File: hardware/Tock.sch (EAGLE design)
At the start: 37 parts, among them IC1 NE555D, IC2 LM7805, IC3 AVR-MEGA8-PPTH, IC4 MCP1700-33, J2 ISP, J4 VIN, Y1 16MHz

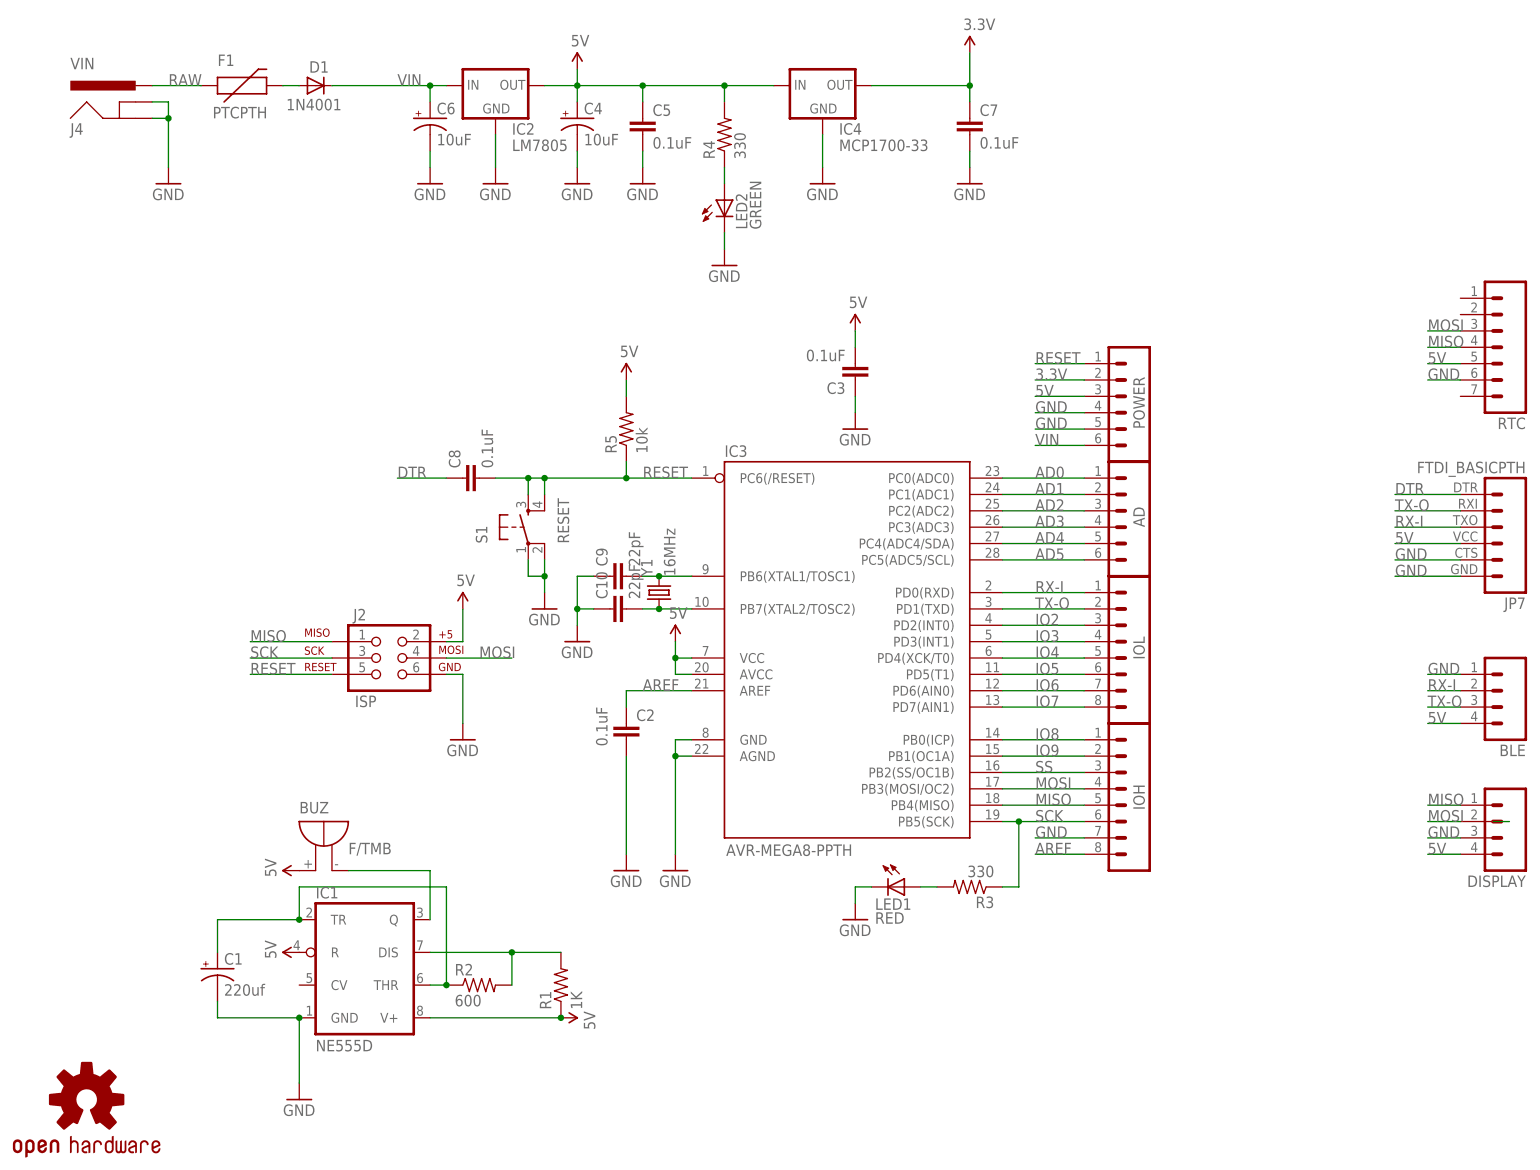
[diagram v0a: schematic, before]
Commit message: Update hardware
Remove extra bit-packing code and switch to standard library macros
Encapsulate enums
Add WIP BOM and more information to readme
Finish routing hardware
Switch to SMD capacitors and resistors
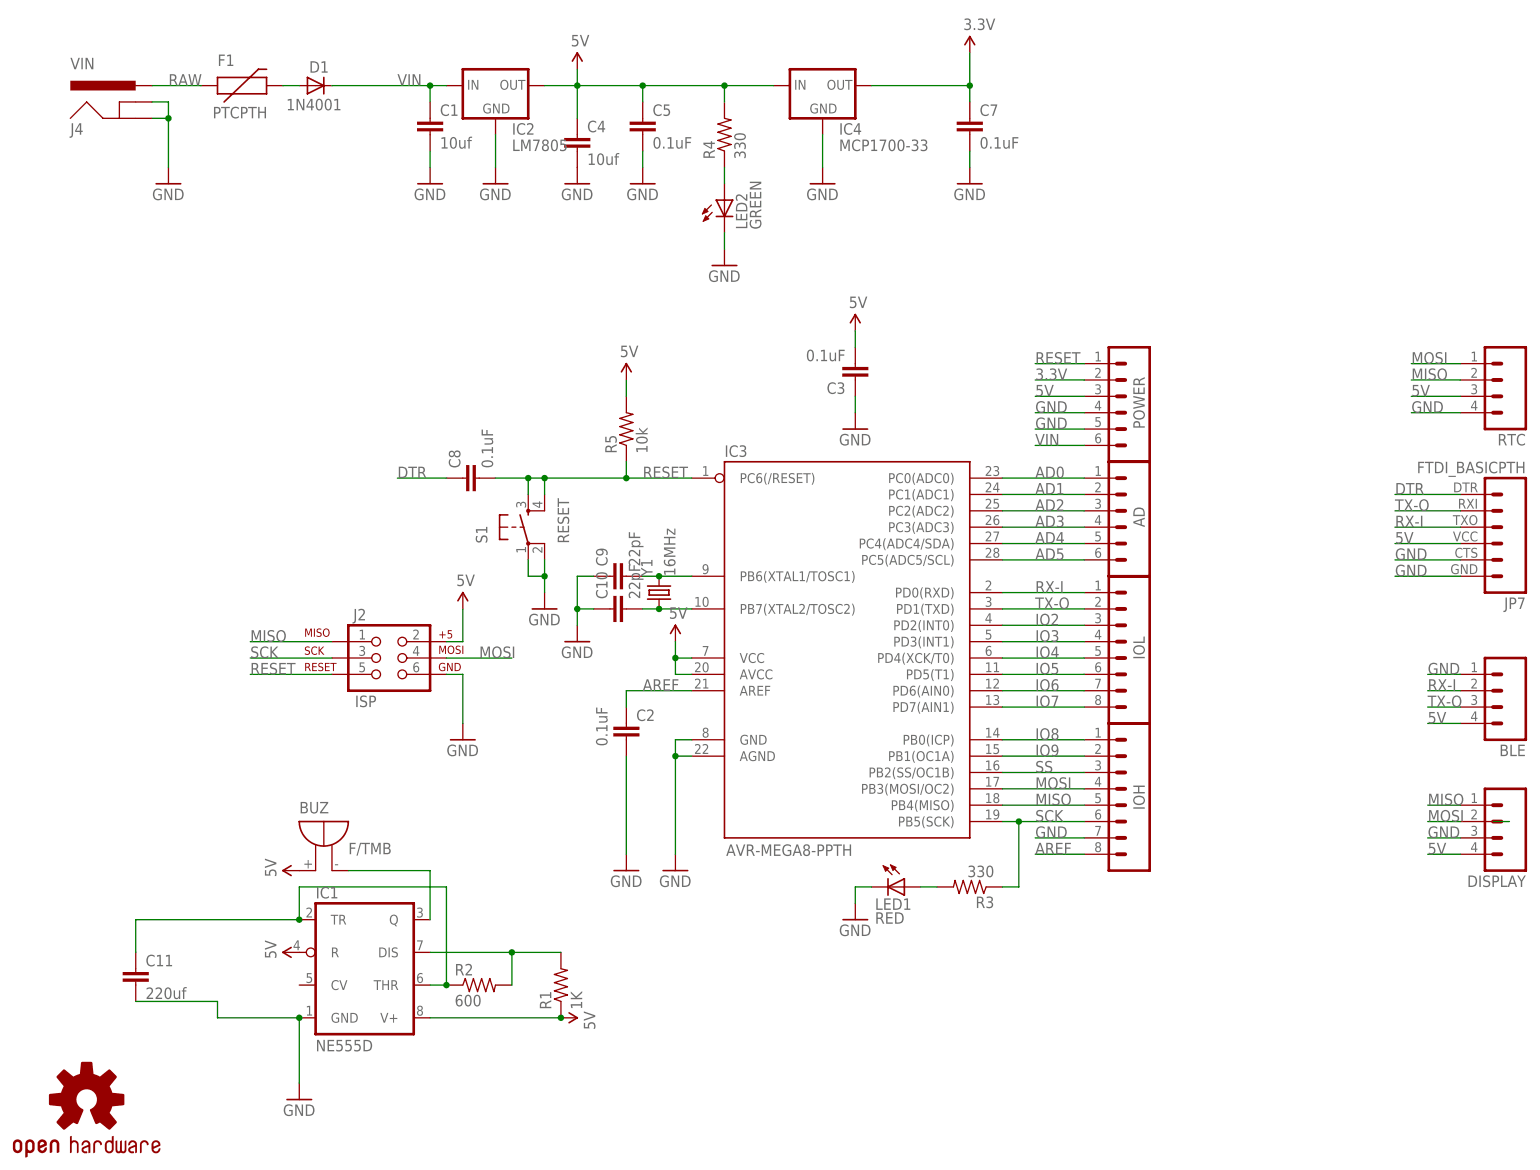
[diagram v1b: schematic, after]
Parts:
- removed C6: 10uF, SparkFun:CAP_POLPTH2
- added C11: 220uf, SparkFun-Passives:CAP0805
- AD, POWER: device SparkFun:M06SIP -> SparkFun-Connectors:M06LOCK
- C1: value 220uf -> 10uf; device rcl:CPOL-USE2.5-5 -> SparkFun-Passives:CAP0805
- C10, C2, C5, C7, C8, C9: device SparkFun:CAPPTH2 -> SparkFun-Passives:CAP0805
- C4: value 10uF -> 10uf; device SparkFun:CAP_POLPTH2 -> SparkFun-Passives:CAP0805
- IOH, IOL: device SparkFun:M081X08 -> SparkFun-Connectors:M08LOCK
- LED1, LED2: device SparkFun:LED5MM -> led:LEDCHIP-LED0805
- R1, R2: device rcl:R-US_0204/5 -> SparkFun-Resistors:RESISTOR0805-RES
- R3, R4, R5: device SparkFun:RESISTORAXIAL-0.3 -> SparkFun-Resistors:RESISTOR0805-RES
- RTC: device SparkFun-Connectors:M07LOCK -> SparkFun-Connectors:M04LOCK
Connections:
- net 5V: now also C4.1, RTC.3; no longer C4.+, RTC.5
- net GND: now also C1.2, C11.2, C4.2, RTC.4; no longer C1.-, C4.-, C6.-, RTC.6
- net MISO: now also RTC.2; no longer RTC.4
- net MOSI: now also RTC.1; no longer RTC.3
- net N$5: now also C11.1; no longer C1.+
- net VIN: now also C1.1; no longer C6.+

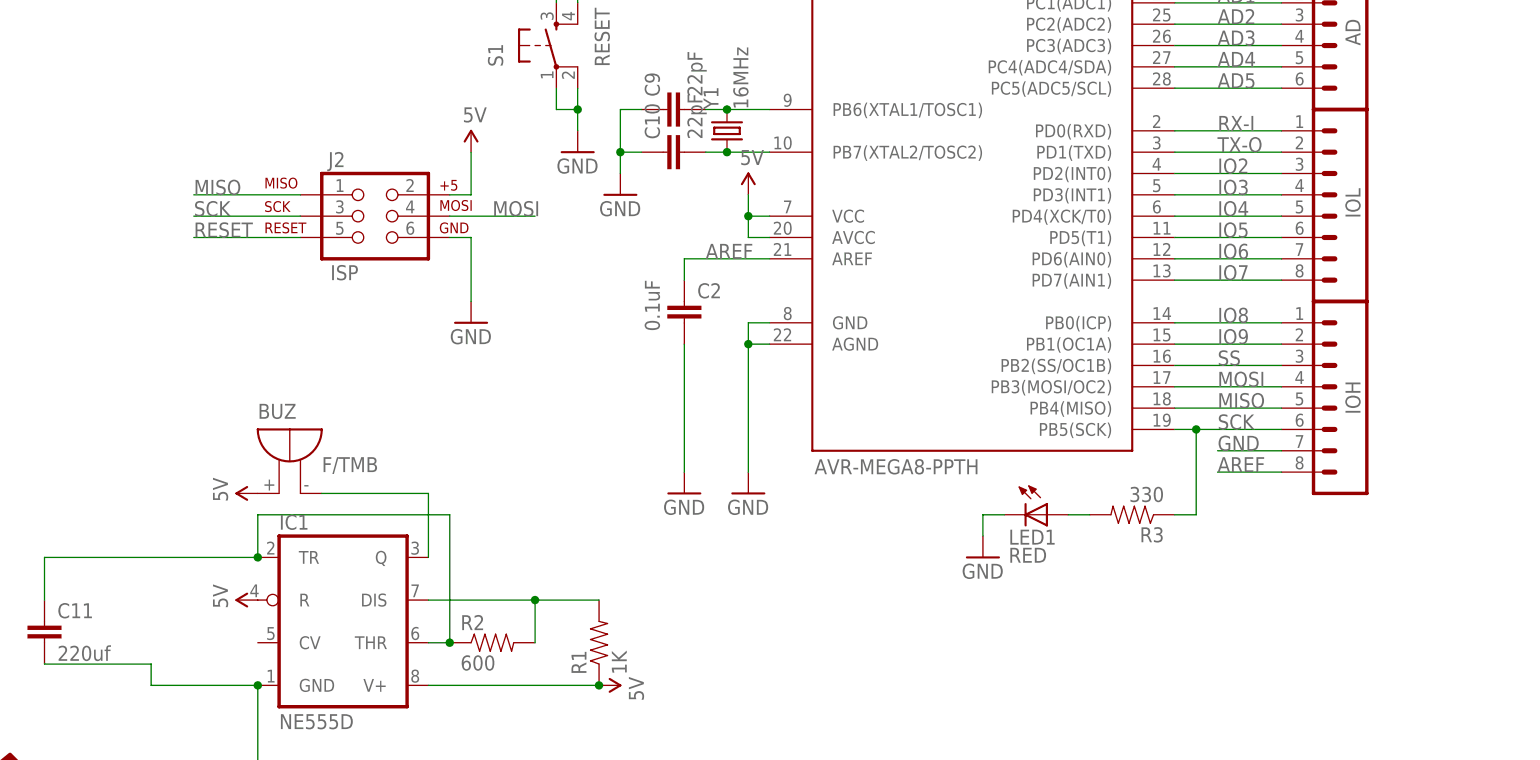
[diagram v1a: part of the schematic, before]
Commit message: Shrink board footprint further
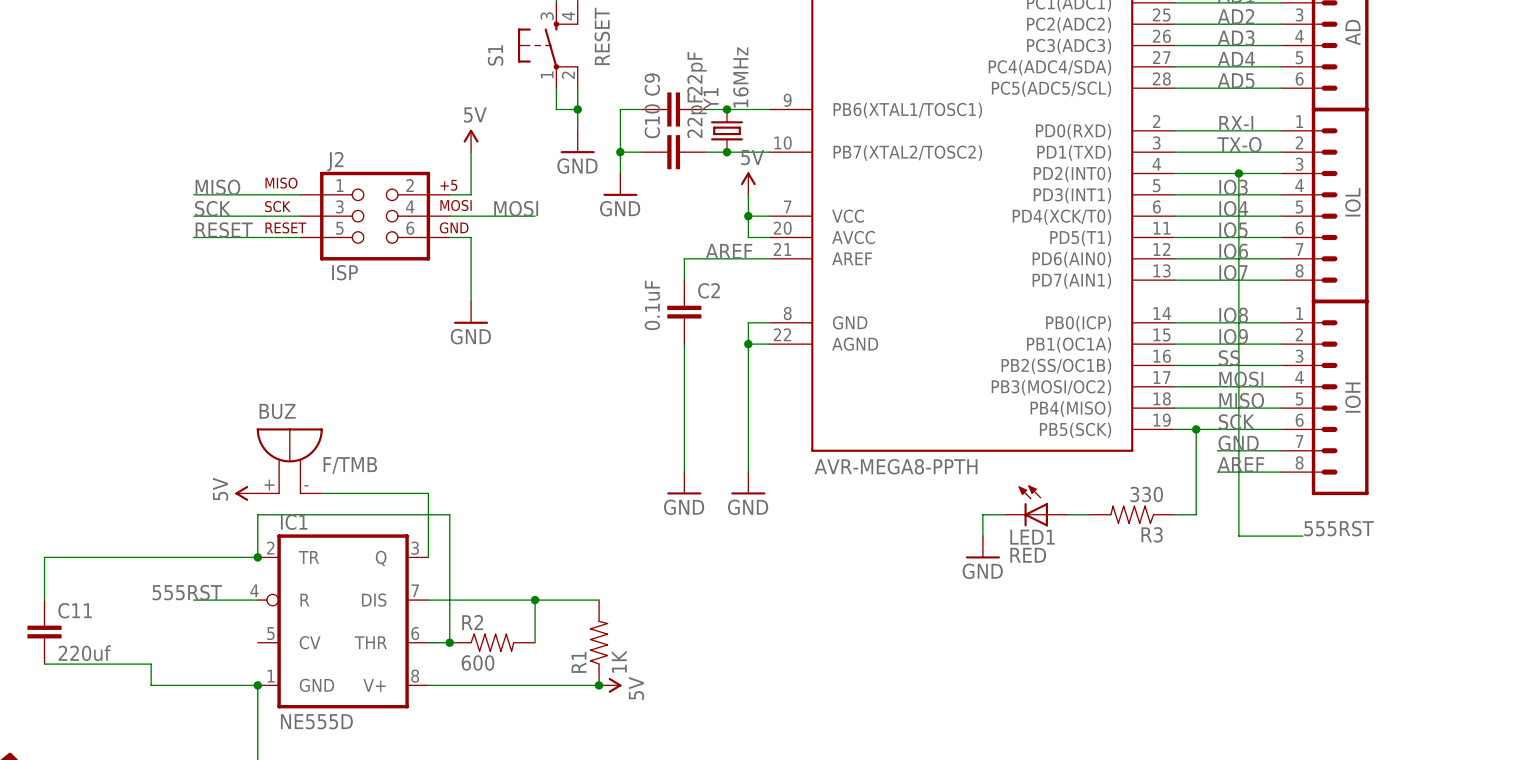
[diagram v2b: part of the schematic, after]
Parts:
- C3: device SparkFun:CAPPTH2 -> SparkFun-Capacitors:1.0UF-25V-+80/-20(0805)
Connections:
- removed net IO2: IC3.PD2(INT0), IOL.3
- new net 555RST: IC1.R, IC3.PD2(INT0), IOL.3
- net 5V: no longer IC1.R
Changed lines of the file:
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@@
 <part name="GND6" library="SparkFun" deviceset="GND" device=""/>
 <part name="U$4" library="SparkFun" deviceset="5V" device=""/>
-<part name="C3" library="SparkFun" deviceset="CAP" device="PTH2" value="0.1uF"/>
+<part name="C3" library="SparkFun-Capacitors" deviceset="1.0UF-25V-+80/-20(0805)" device="" value="0.1uF"/>
 <part name="GND7" library="SparkFun" deviceset="GND" device=""/>
 <part name="GND8" library="SparkFun" deviceset="GND" device=""/>
@@
 <part name="U$2" library="SparkFun" deviceset="5V" device=""/>
 <part name="GND14" library="SparkFun" deviceset="GND" device=""/>
-<part name="U$8" library="SparkFun" deviceset="5V" device=""/>
 <part name="U$9" library="SparkFun" deviceset="5V" device=""/>
 <part name="BLE" library="SparkFun-Connectors" deviceset="M04" device="LOCK"/>
@@
 <instance part="U$2" gate="G$1" x="-27.94" y="-60.96" rot="R270"/>
 <instance part="GND14" gate="1" x="-68.58" y="-73.66"/>
-<instance part="U$8" gate="G$1" x="-68.58" y="-50.8" rot="R90"/>
 <instance part="U$9" gate="G$1" x="-68.58" y="-38.1" rot="R90"/>
 <instance part="BLE" gate="G$1" x="116.84" y="-10.16" rot="R180"/>
@@
 <wire x1="106.68" y1="-10.16" x2="111.76" y2="-10.16" width="0.1524" layer="91"/>
 <label x="106.68" y="-10.16" size="1.778" layer="95"/>
-</segment>
-</net>
-<net name="IO2" class="2">
-<segment>
-<wire x1="53.34" y1="0" x2="40.64" y2="0" width="0.1524" layer="91"/>
-<label x="45.72" y="0" size="1.778" layer="95"/>
-<pinref part="IOL" gate="G$1" pin="3"/>
-<pinref part="IC3" gate="G$1" pin="PD2(INT0)"/>
 </segment>
 </net>
@@
 </segment>
 <segment>
-<pinref part="IC1" gate="A" pin="R"/>
-<pinref part="U$8" gate="G$1" pin="5V"/>
-</segment>
-<segment>
 <pinref part="BUZ" gate="1" pin="+"/>
 <pinref part="U$9" gate="G$1" pin="5V"/>
@@
 </segment>
 </net>
+<net name="555RST" class="0">
+<segment>
+<pinref part="IC1" gate="A" pin="R"/>
+<wire x1="-68.58" y1="-50.8" x2="-76.2" y2="-50.8" width="0.1524" layer="91"/>
+<label x="-81.28" y="-50.8" size="1.778" layer="95"/>
+</segment>
+<segment>
+<wire x1="53.34" y1="0" x2="48.26" y2="0" width="0.1524" layer="91"/>
+<label x="55.88" y="-43.18" size="1.778" layer="95"/>
+<pinref part="IOL" gate="G$1" pin="3"/>
+<pinref part="IC3" gate="G$1" pin="PD2(INT0)"/>
+<junction x="48.26" y="0"/>
+<wire x1="48.26" y1="0" x2="40.64" y2="0" width="0.1524" layer="91"/>
+<wire x1="48.26" y1="0" x2="48.26" y2="-43.18" width="0.1524" layer="91"/>
+<wire x1="48.26" y1="-43.18" x2="55.88" y2="-43.18" width="0.1524" layer="91"/>
+</segment>
+</net>
